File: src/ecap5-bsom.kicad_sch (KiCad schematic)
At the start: 0 parts

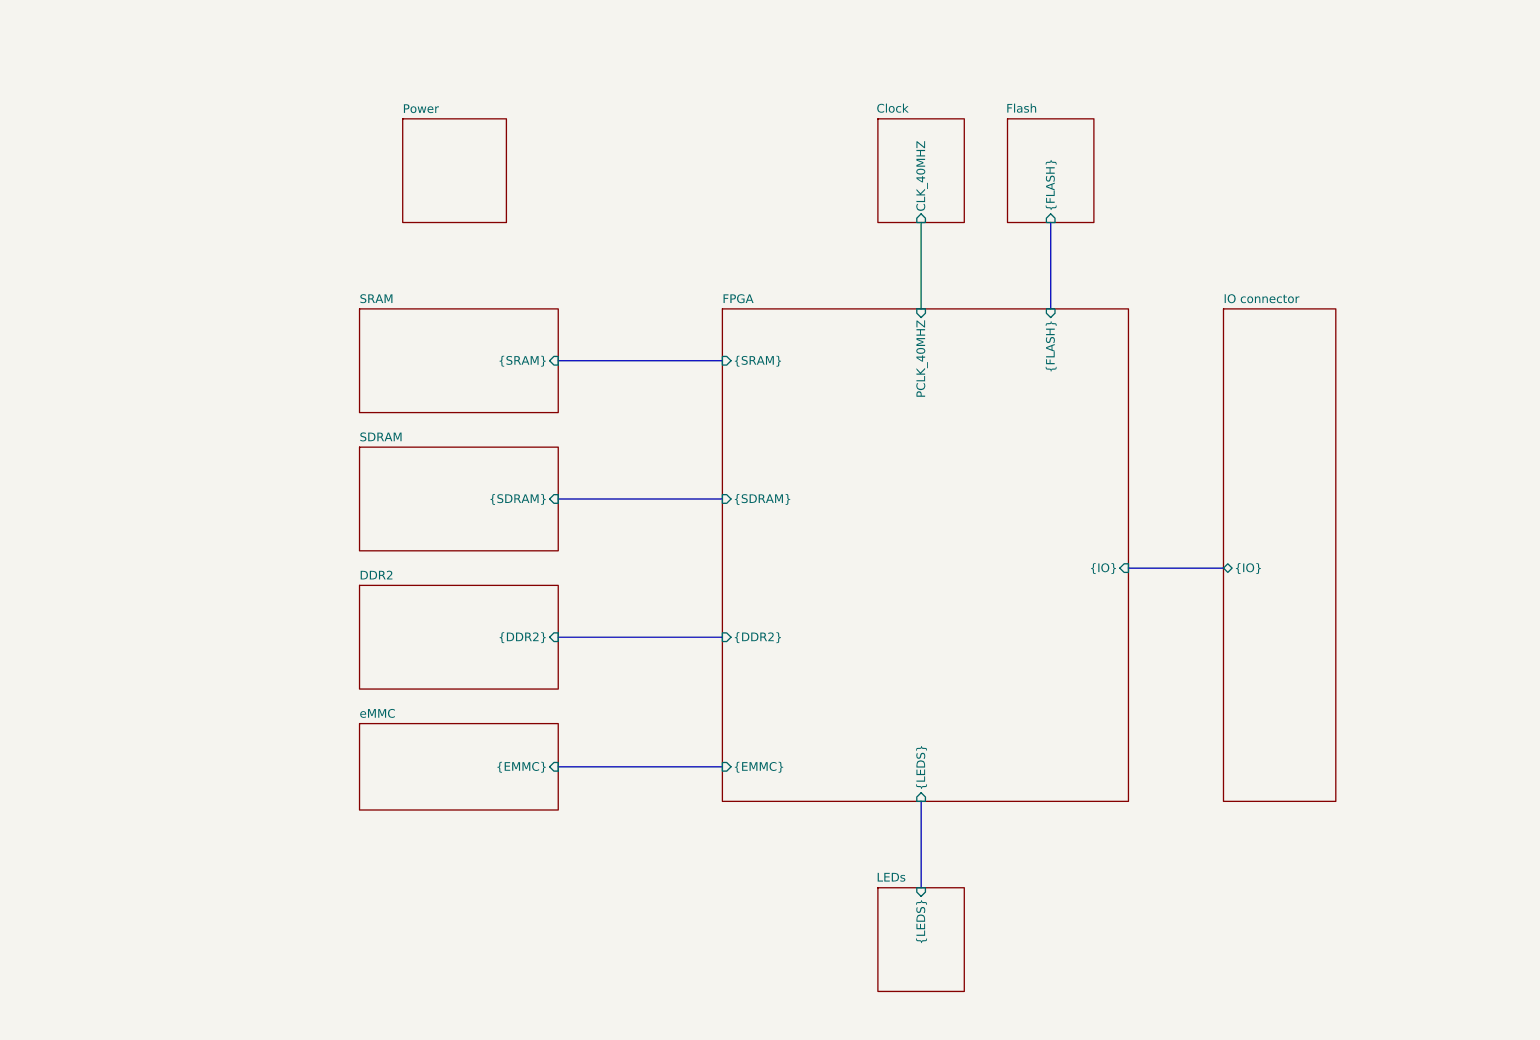
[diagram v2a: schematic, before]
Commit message: Remove bus groups
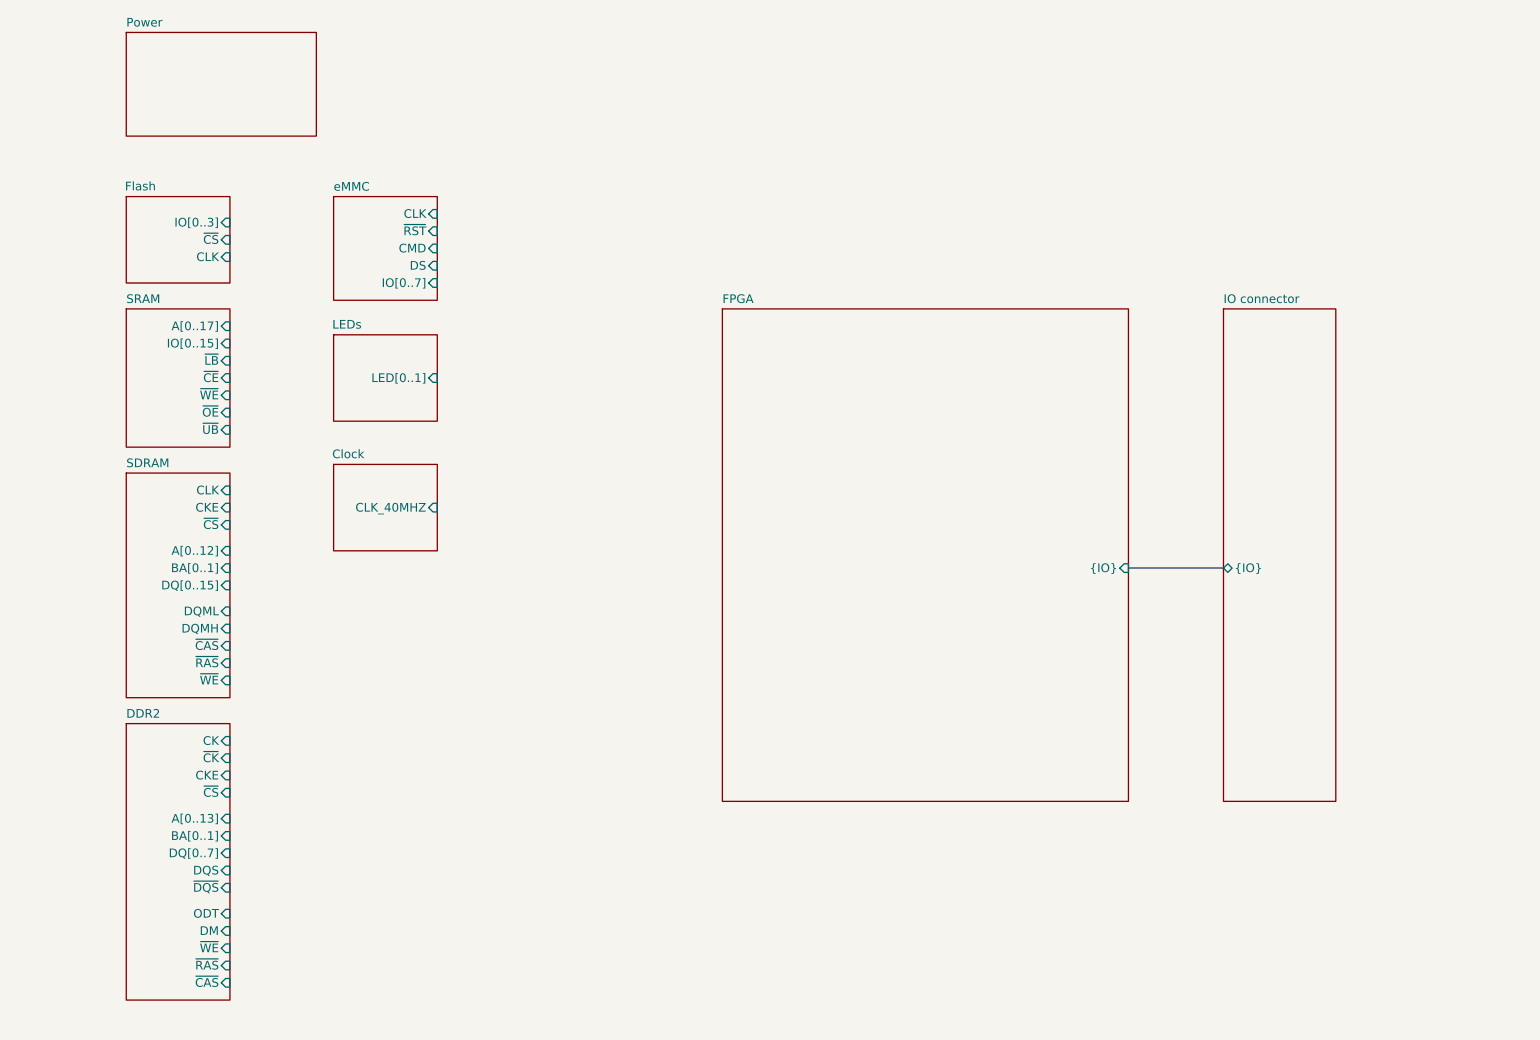
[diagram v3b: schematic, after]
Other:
- sheet DDR2 ports: added A[0..13], BA[0..1], CK, CKE, DM, DQS, DQ[0..7], ODT, ~{CAS}, ~{CK}, ~{CS}, ~{DQS}, ~{RAS}, ~{WE}; removed {DDR2}
- sheet FPGA ports: added none; removed PCLK_40MHZ, {DDR2}, {EMMC}, {FLASH}, {LEDS}, {SDRAM}, {SRAM}
- sheet Flash ports: added CLK, IO[0..3], ~{CS}; removed {FLASH}
- sheet LEDs ports: added LED[0..1]; removed {LEDS}
- sheet SDRAM ports: added A[0..12], BA[0..1], CKE, CLK, DQMH, DQML, DQ[0..15], ~{CAS}, ~{CS}, ~{RAS}, ~{WE}; removed {SDRAM}
- sheet SRAM ports: added A[0..17], IO[0..15], ~{CE}, ~{LB}, ~{OE}, ~{UB}, ~{WE}; removed {SRAM}
- sheet eMMC ports: added CLK, CMD, DS, IO[0..7], ~{RST}; removed {EMMC}

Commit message: Updates the root page
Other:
- removed sheet FPGA
- added sheet FPGA Bank 0 (fpga-bank0.kicad_sch)
- added sheet FPGA Bank 1 (fpga-bank1.kicad_sch)
- added sheet FPGA Bank 2 (fpga-bank2.kicad_sch)
- added sheet FPGA Bank 3 (fpga-bank3.kicad_sch)
- added sheet FPGA Bank 4 (fpga-bank4.kicad_sch)
- added sheet FPGA Bank 6 (fpga-bank6.kicad_sch)
- added sheet FPGA Bank 7 (fpga-bank7.kicad_sch)
- added sheet FPGA Bank 8 (fpga-bank8.kicad_sch)
- added sheet JTAG (schematics/jtag.kicad_sch)
- sheet Power: file schematics/power.kicad_sch -> schematics/fpga-power.kicad_sch
- note added: "Lattice ECP5"

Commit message: Finishes the root page
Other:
- sheet JTAG renamed FPGA JTAG
- added sheet FPGA Power (schematics/fpga-power.kicad_sch)
- sheet FPGA Bank 0: file fpga-bank0.kicad_sch -> schematics/fpga-bank0.kicad_sch
- sheet FPGA Bank 0 ports: added SDRAM.A[0..12], SDRAM.BA[0..1], SDRAM.CKE, SDRAM.CLK, SDRAM.DQMH, SDRAM.DQML, SDRAM.DQ[0..15], SDRAM.~{CAS}, SDRAM.~{CS}, SDRAM.~{RAS}, SDRAM.~{WE}; removed A[0..12], BA[0..1], CKE, CLK, DQMH, DQML, DQ[0..15], ~{CAS}, ~{CS}, ~{RAS}, ~{WE}
- sheet FPGA Bank 1: file fpga-bank1.kicad_sch -> schematics/fpga-bank1.kicad_sch
- sheet FPGA Bank 1 ports: added SRAM.A[0..17], SRAM.IO[0..15], SRAM.~{CE}, SRAM.~{LB}, SRAM.~{OE}, SRAM.~{UB}, SRAM.~{WE}; removed SRAM_A[0..17], SRAM_IO[0..15], SRAM_~{CE}, SRAM_~{LB}, SRAM_~{OE}, SRAM_~{UB}, SRAM_~{WE}
- sheet FPGA Bank 2: file fpga-bank2.kicad_sch -> schematics/fpga-bank2.kicad_sch
- sheet FPGA Bank 3: file fpga-bank3.kicad_sch -> schematics/fpga-bank3.kicad_sch
- sheet FPGA Bank 4: file fpga-bank4.kicad_sch -> schematics/fpga-bank4.kicad_sch
- sheet FPGA Bank 6: file fpga-bank6.kicad_sch -> schematics/fpga-bank6.kicad_sch
- sheet FPGA Bank 7: file fpga-bank7.kicad_sch -> schematics/fpga-bank7.kicad_sch
- sheet FPGA Bank 7 ports: added DDR2.A[0..13], DDR2.BA[0..1], DDR2.CK, DDR2.CKE, DDR2.DM, DDR2.DQS, DDR2.DQ[0..7], DDR2.ODT, DDR2.~{CAS}, DDR2.~{CK}, DDR2.~{CS}, DDR2.~{DQS}, DDR2.~{RAS}, DDR2.~{WE}, EMMC.CLK, EMMC.CMD, EMMC.DS, EMMC.IO[0..7], EMMC.~{RST}; removed EMMC_CLK, EMMC_CMD, EMMC_DS, EMMC_IO[0..7], EMMC_~{RST}
- sheet FPGA Bank 8: file fpga-bank8.kicad_sch -> schematics/fpga-bank8.kicad_sch
- sheet Power: file schematics/fpga-power.kicad_sch -> schematics/power.kicad_sch

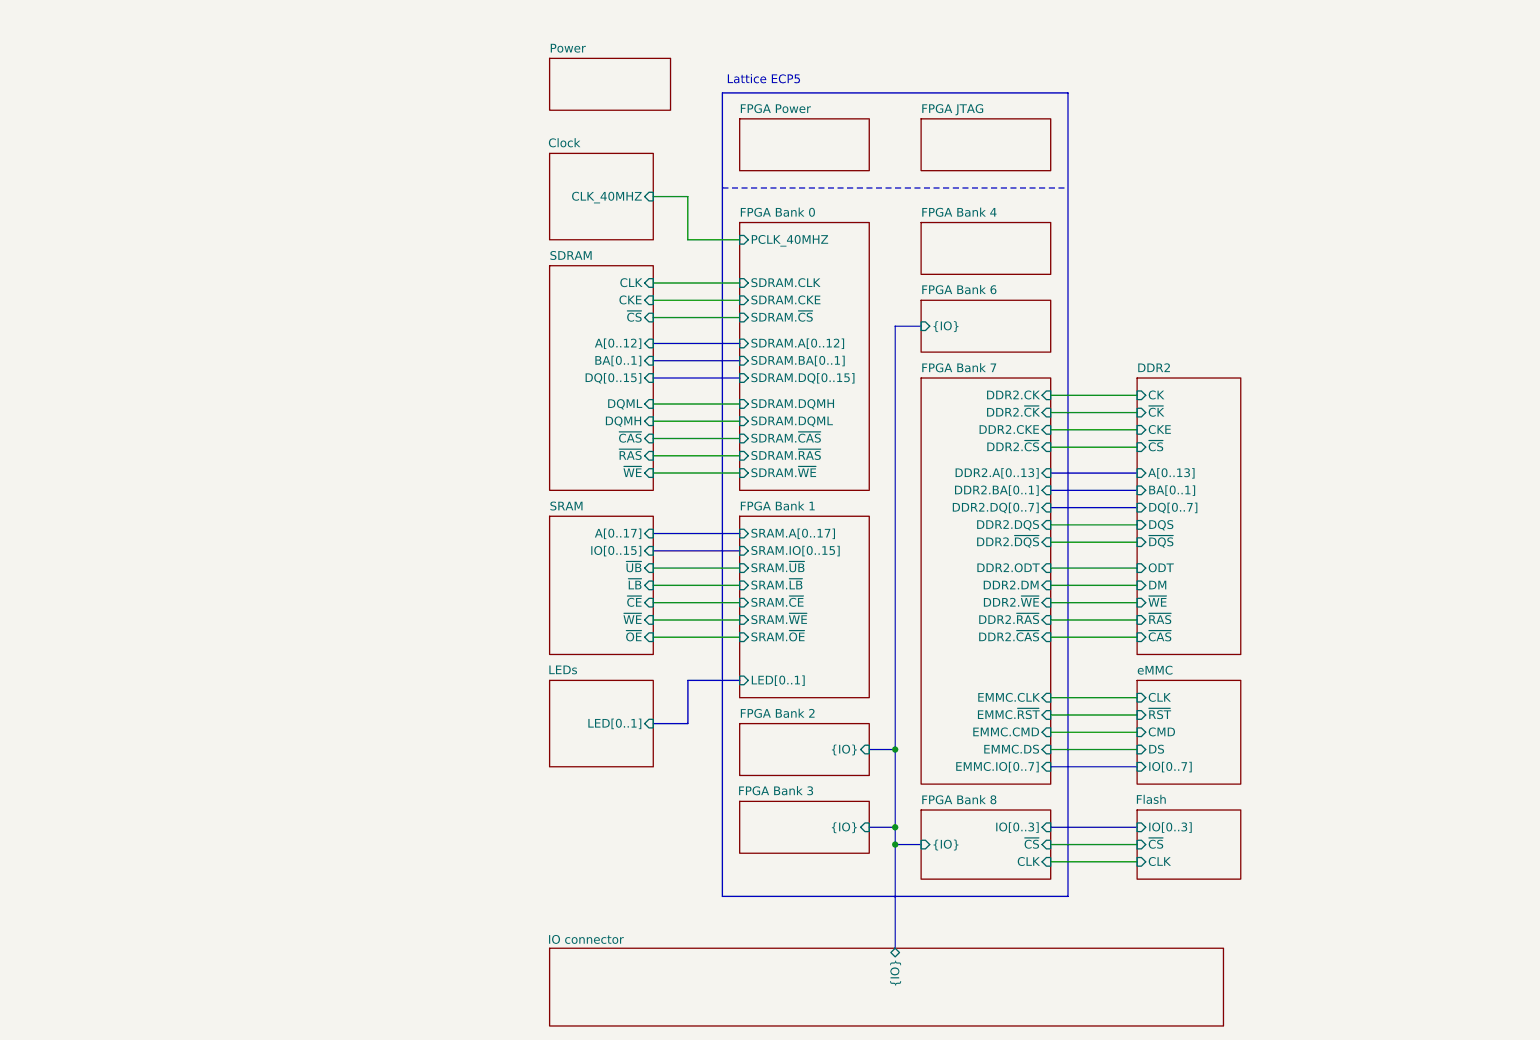
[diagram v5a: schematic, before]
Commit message: Adds a revision history table
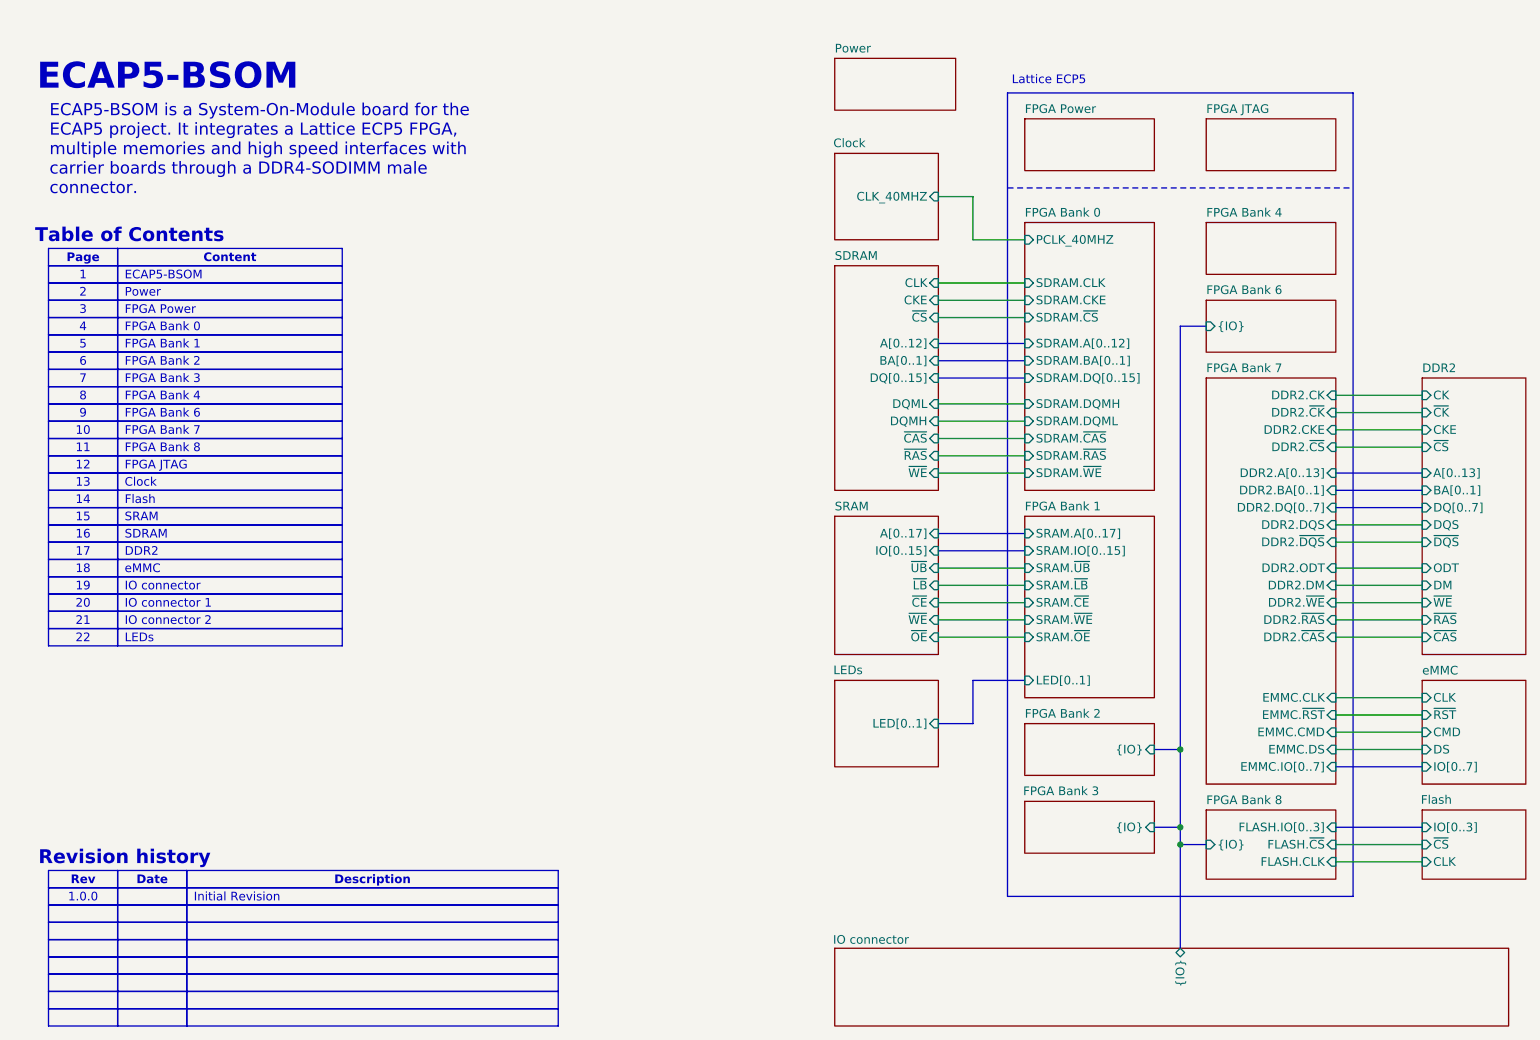
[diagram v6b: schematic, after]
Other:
- sheet FPGA Bank 8 ports: added FLASH.CLK, FLASH.IO[0..3], FLASH.~{CS}; removed CLK, IO[0..3], ~{CS}
- note added: "ECAP5-BSOM"
- note added: "Revision history"
- note added: "Table of Contents"

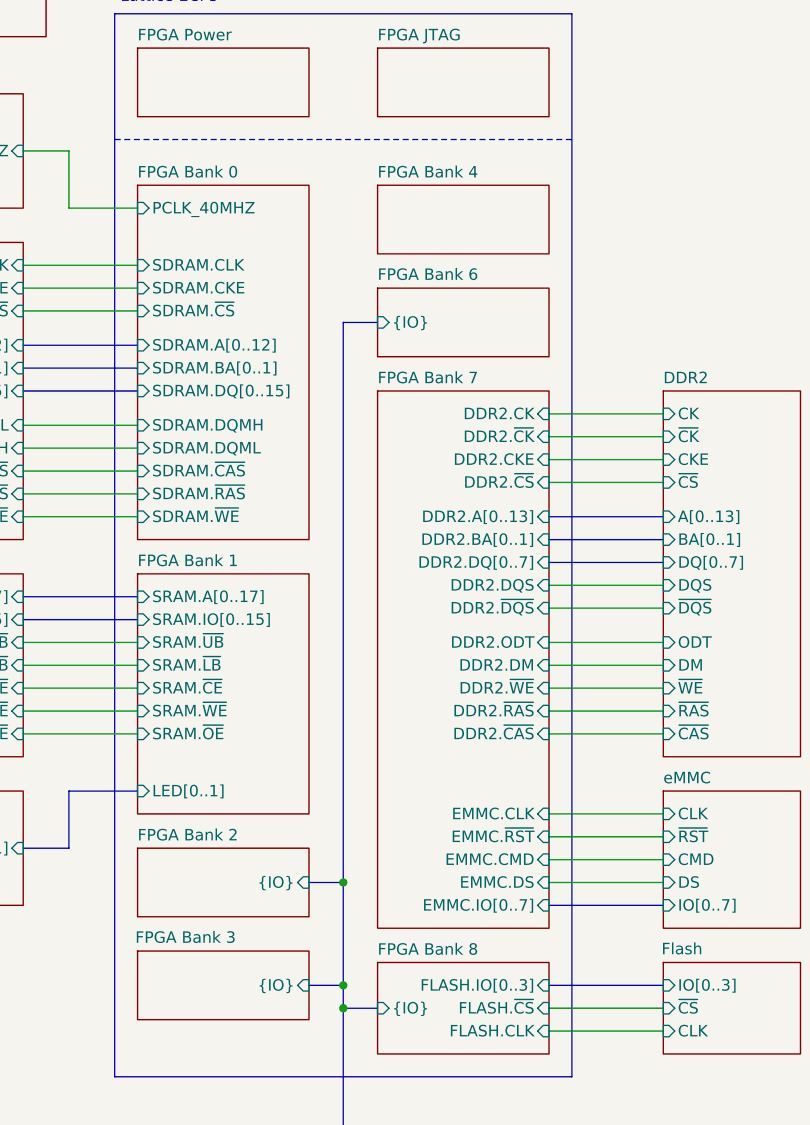
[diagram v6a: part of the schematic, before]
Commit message: Fixes ERC issues
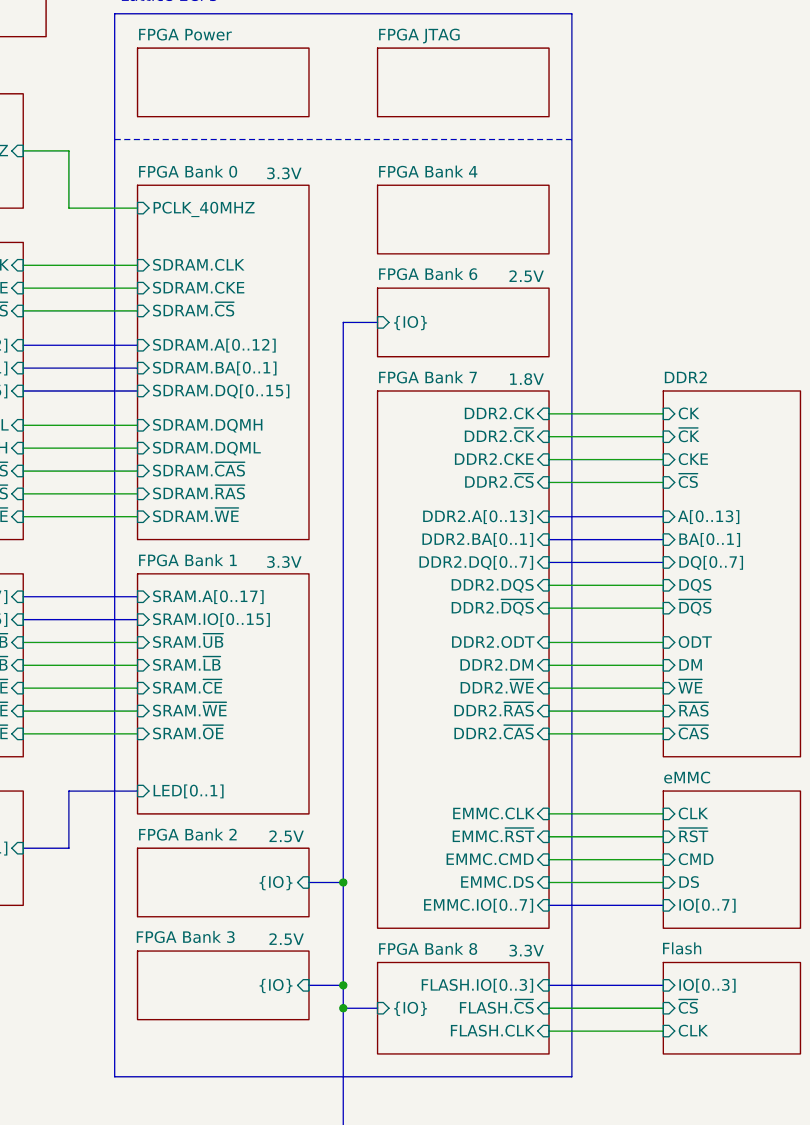
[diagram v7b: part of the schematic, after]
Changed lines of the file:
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@@
 		(at 168.91 91.44)
 		(size 19.05 26.67)
-		(fields_autoplaced yes)
 		(stroke
 			(width 0.1524)
@@
 			)
 		)
+		(property "Vio" "3.3V"
+			(at 185.166 90.17 0)
+			(do_not_autoplace yes)
+			(effects
+				(font
+					(size 1.27 1.27)
+				)
+			)
+		)
 		(pin "LED[0..1]" input
 			(at 168.91 115.57 180)
@@
 		(at 195.58 134.62)
 		(size 19.05 10.16)
-		(fields_autoplaced yes)
 		(stroke
 			(width 0.1524)
@@
 				(justify left top)
 				(hide yes)
+			)
+		)
+		(property "Vio" "3.3V"
+			(at 212.09 133.35 0)
+			(effects
+				(font
+					(size 1.27 1.27)
+				)
 			)
 		)
@@
 			)
 		)
+		(property "Vio" "2.5V"
+			(at 212.09 58.42 0)
+			(effects
+				(font
+					(size 1.27 1.27)
+				)
+			)
+		)
 		(pin "{IO}" input
 			(at 195.58 63.5 180)
@@
 		(at 168.91 48.26)
 		(size 19.05 39.37)
-		(fields_autoplaced yes)
 		(stroke
 			(width 0.1524)
@@
 				(justify left top)
 				(hide yes)
+			)
+		)
+		(property "Vio" "3.3V"
+			(at 185.166 46.99 0)
+			(effects
+				(font
+					(size 1.27 1.27)
+				)
 			)
 		)
@@
 		(at 168.91 121.92)
 		(size 19.05 7.62)
-		(fields_autoplaced yes)
 		(stroke
 			(width 0.1524)
@@
 				(justify left top)
 				(hide yes)
+			)
+		)
+		(property "Vio" "2.5V"
+			(at 185.42 120.65 0)
+			(effects
+				(font
+					(size 1.27 1.27)
+				)
 			)
 		)
@@
 			)
 		)
+		(property "Vio" "2.5V"
+			(at 185.42 132.08 0)
+			(effects
+				(font
+					(size 1.27 1.27)
+				)
+			)
+		)
 		(pin "{IO}" input
 			(at 187.96 137.16 0)
@@
 		(at 195.58 71.12)
 		(size 19.05 59.69)
-		(fields_autoplaced yes)
 		(stroke
 			(width 0.1524)
@@
 			)
 		)
+		(property "Vio" "1.8V"
+			(at 212.09 69.85 0)
+			(effects
+				(font
+					(size 1.27 1.27)
+				)
+			)
+		)
